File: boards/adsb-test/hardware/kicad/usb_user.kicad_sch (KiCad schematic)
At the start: 10 parts, among them U901 CP2102N-A02-GQFN24

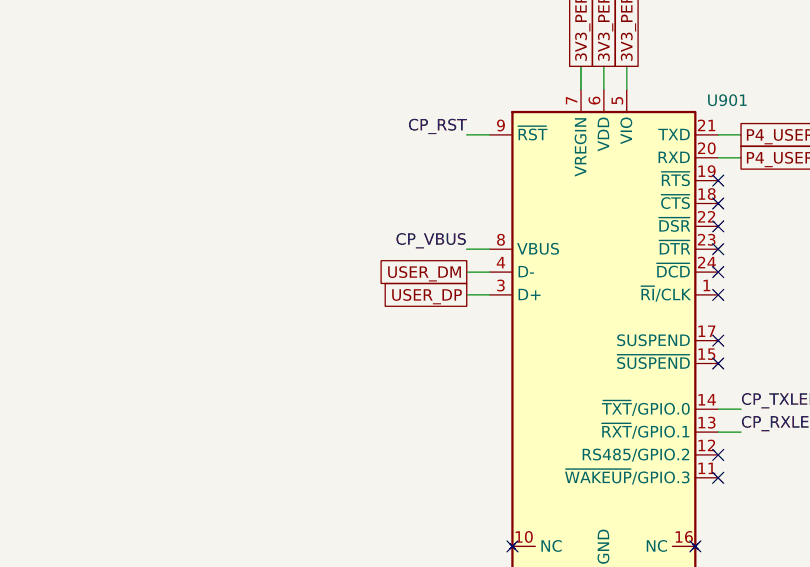
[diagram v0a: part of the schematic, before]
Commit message: ADSB_Test: net classes + diff-pair rules, USB pairs renamed _D_P/_D_N, U201 VSYS drawn at the bottom
Co-Authored-By: Claude Opus 5.5 <noreply@anthropic.com>
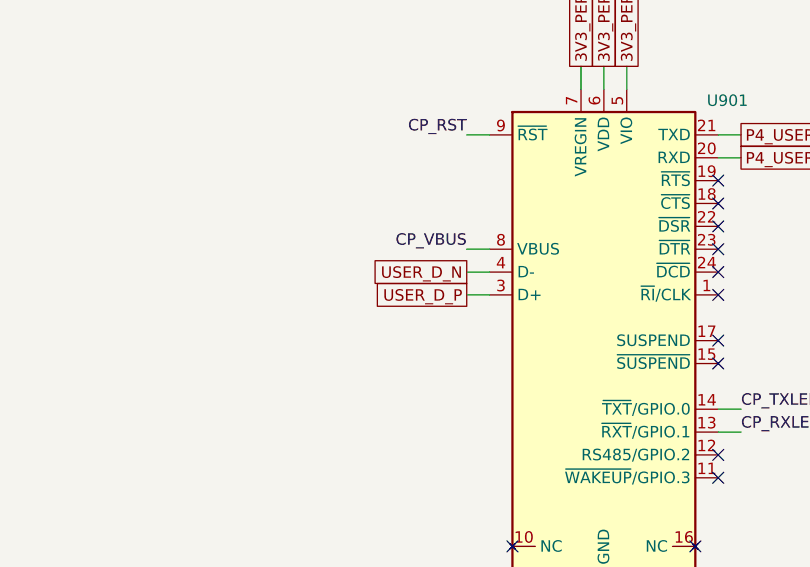
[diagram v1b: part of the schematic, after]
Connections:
- net USER_DM renamed USER_D_N
- net USER_DP renamed USER_D_P

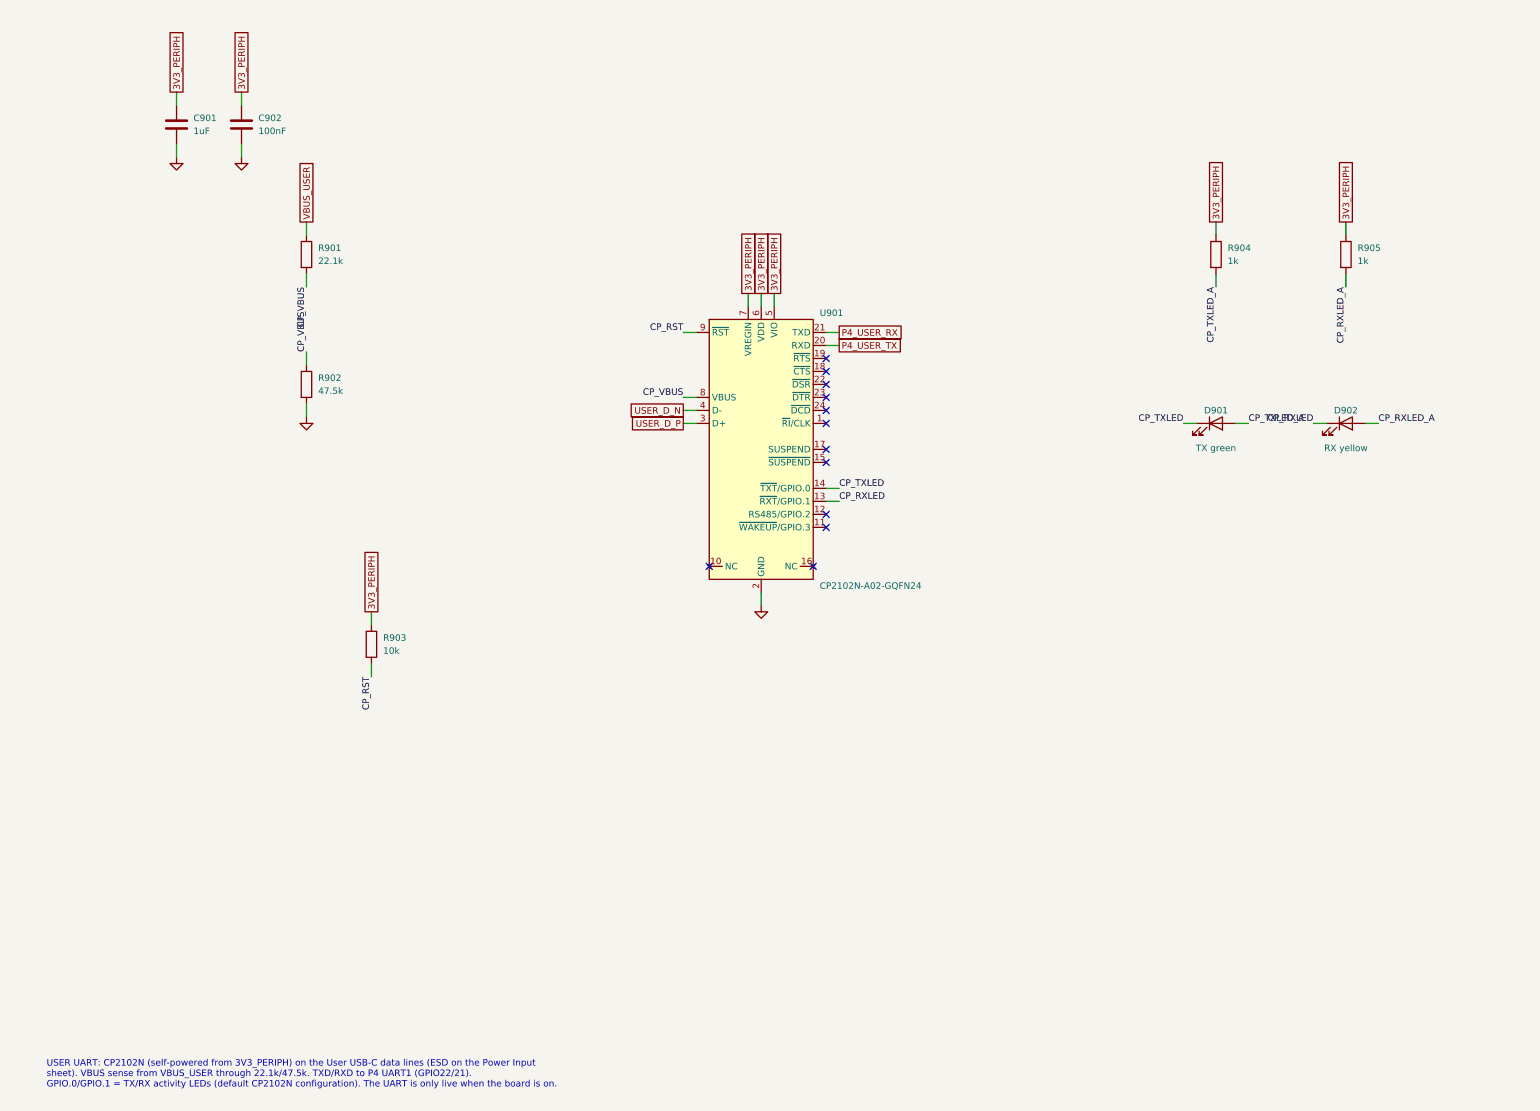
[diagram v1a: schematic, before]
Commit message: ADSB_Test: User USB-C on its own sheet, RP2040 GPIO header + optional I2C, shunt/PWR_FLAG text fixed
Co-Authored-By: Claude Opus 5.5 <noreply@anthropic.com>
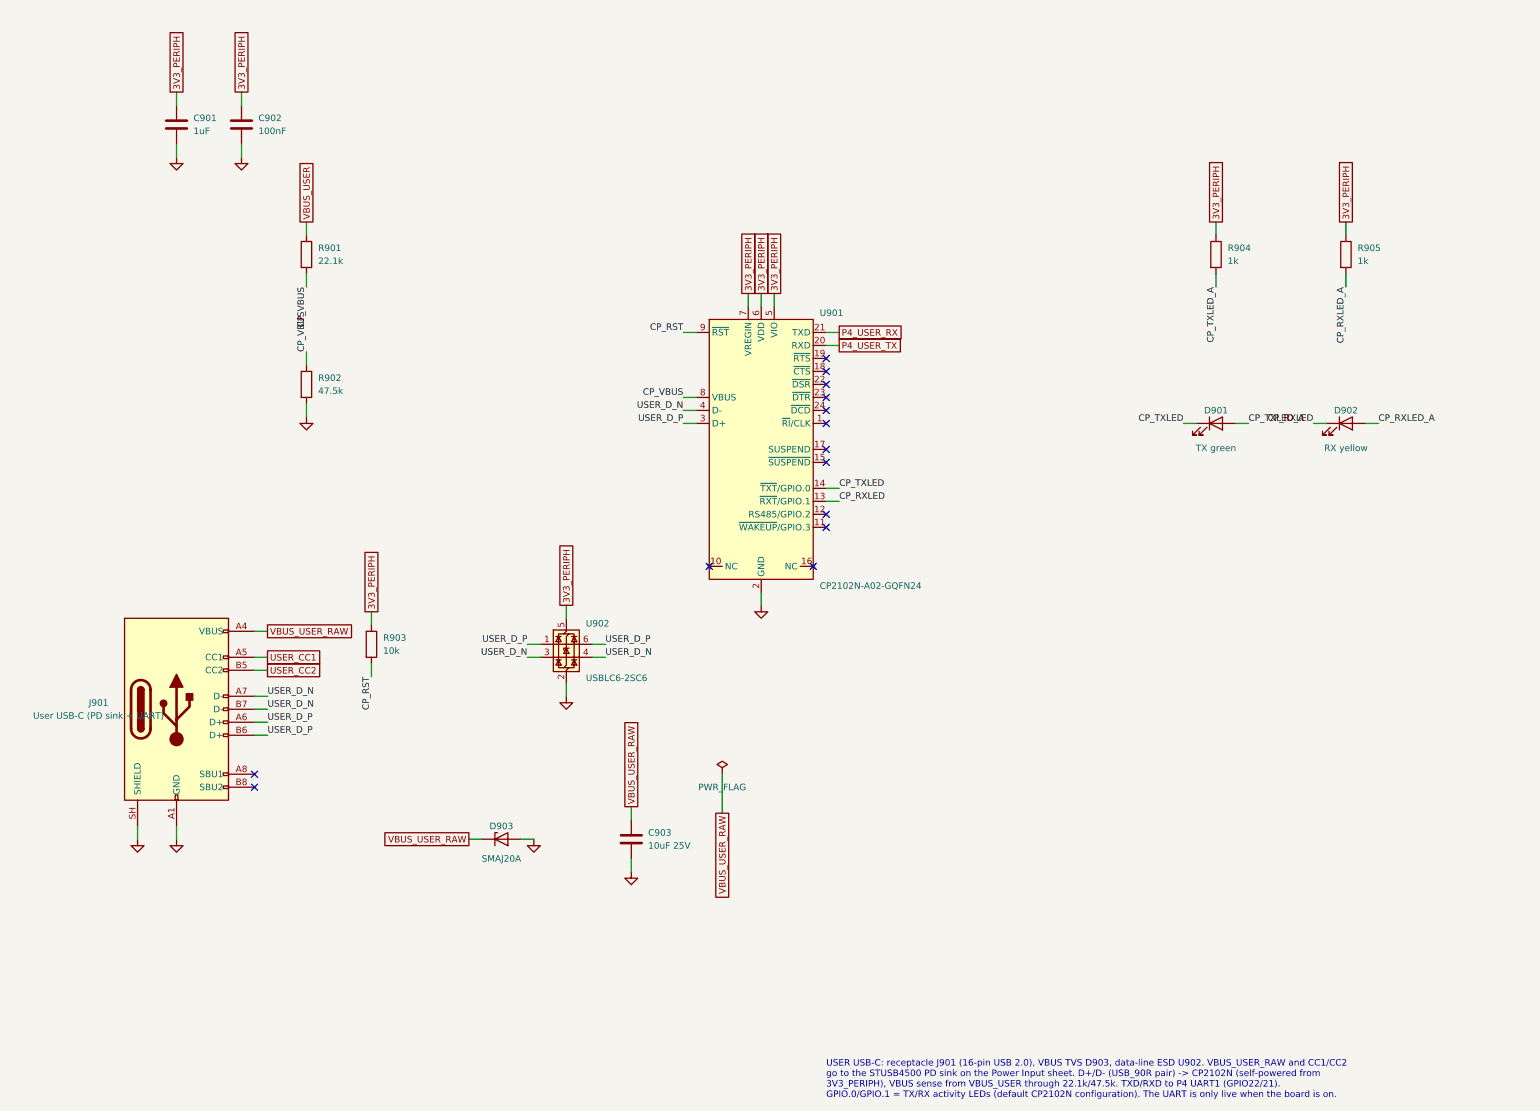
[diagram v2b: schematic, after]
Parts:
- added C903: 10uF 25V, Capacitor_SMD:C_0805_2012Metric_Pad1.18x1.45mm_HandSolder, symbol Device:C
- added D903: SMAJ20A, Diode_SMD:D_SMA, symbol Device:D_Zener
- added J901: User USB-C (PD sink + UART), Connector_USB:USB_C_Receptacle_GCT_USB4105-xx-A_16P_TopMnt_Horizontal, symbol Connector:USB_C_Receptacle_USB2.0_16P
- added U902: USBLC6-2SC6, Package_TO_SOT_SMD:SOT-23-6_Handsoldering, symbol Power_Protection:USBLC6-2SC6
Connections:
- net 3V3_PERIPH: now also U902.5 (VBUS)
- net GND: now also C903.2, D903.2 (A), J901.A1 (GND), J901.A12 (GND), J901.B1 (GND), J901.B12 (GND), J901.SH (SHIELD), U902.2 (GND)
- net USER_D_N: now also J901.A7 (D-), J901.B7 (D-), U902.3 (I/O2), U902.4 (I/O2)
- net USER_D_P: now also J901.A6 (D+), J901.B6 (D+), U902.1 (I/O1), U902.6 (I/O1)
- new net USER_CC1: J901.A5 (CC1)
- new net USER_CC2: J901.B5 (CC2)
- new net VBUS_USER_RAW: C903.1, D903.1 (K), J901.A4 (VBUS), J901.A9 (VBUS), J901.B4 (VBUS), J901.B9 (VBUS)
- no-connect marks 12 -> 14
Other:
- note added: "USER USB-C: receptacle J901 (16-pin USB 2.0), VBUS TVS D903, data-line ESD U902. VBUS_USER_RAW and CC1/CC2 go to the STUSB4500 PD sink on the Power Input sheet. D+/D- (USB_90R pair) -> CP2102N (self-powered from 3V3_PERIPH), VBUS sense from VBUS_USER through 22.1k/47.5k. TXD/RXD to P4 UART1 (GPIO22/21). GPIO.0/GPIO.1 = TX/RX activity LEDs (default CP2102N configuration). The UART is only live whe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"
- note removed: "USER UART: CP2102N (self-powered from 3V3_PERIPH) on the User USB-C data lines (ESD on the Power Input sheet). VBUS sense from VBUS_USER through 22.1k/47.5k. TXD/RXD to P4 UART1 (GPIO22/21). GPIO.0/GPIO.1 = TX/RX activity LEDs (default CP2102N configuration). The UART is only live when the board is on."
- title: ADSB_Test - USB User -> ADSB_Test - User USB-C
